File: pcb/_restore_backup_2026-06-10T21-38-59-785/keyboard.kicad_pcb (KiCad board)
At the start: 2 copper layers, 70 x 84 mm, 25 parts, among them SW1 SW_Push, SW2 SW_Push, SW3 RotaryEncoder_Switch, SW4 SW_Push, SW5 SW_Push, SW6 SW_Push, SW7 SW_Push, SW8 SW_Push, SW9 SW_Push, U1 MODULE-SEEEDUINO-XIAO-RP2040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

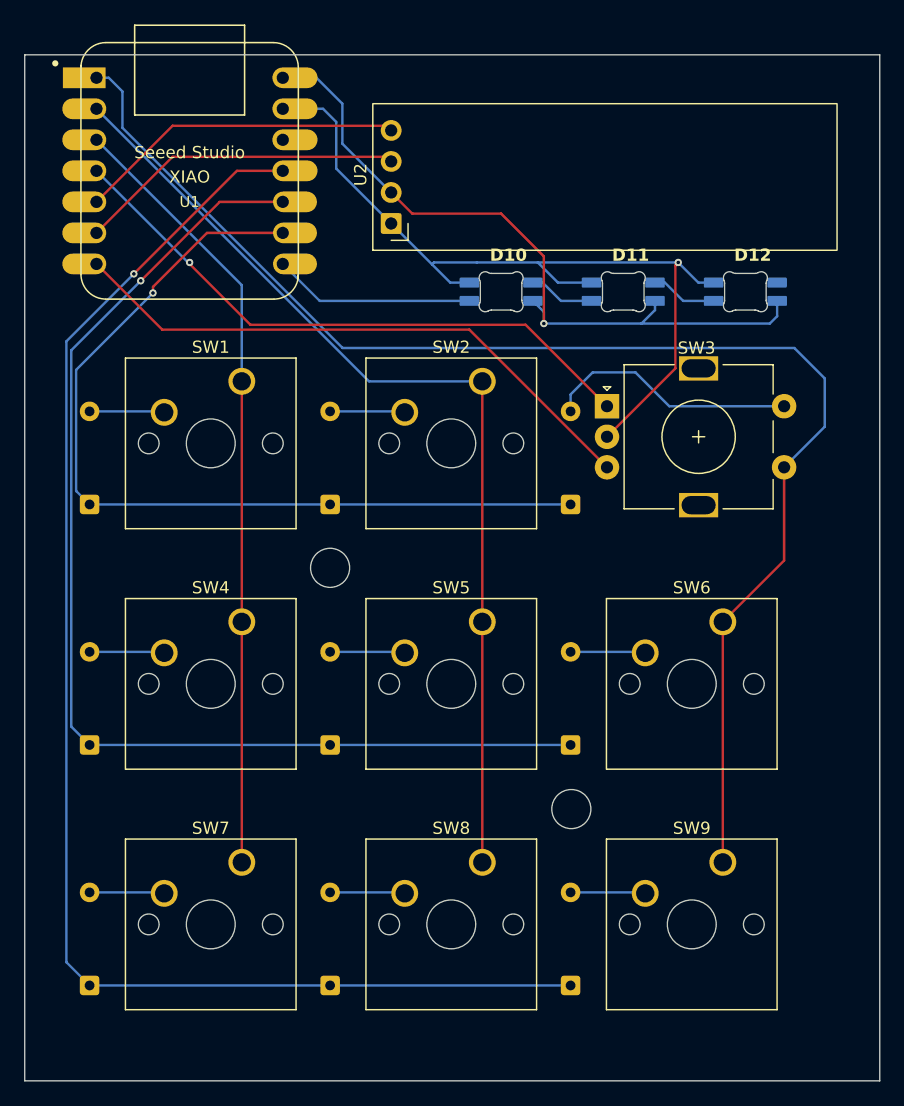
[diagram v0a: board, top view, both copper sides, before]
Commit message: connect everything on the pcb
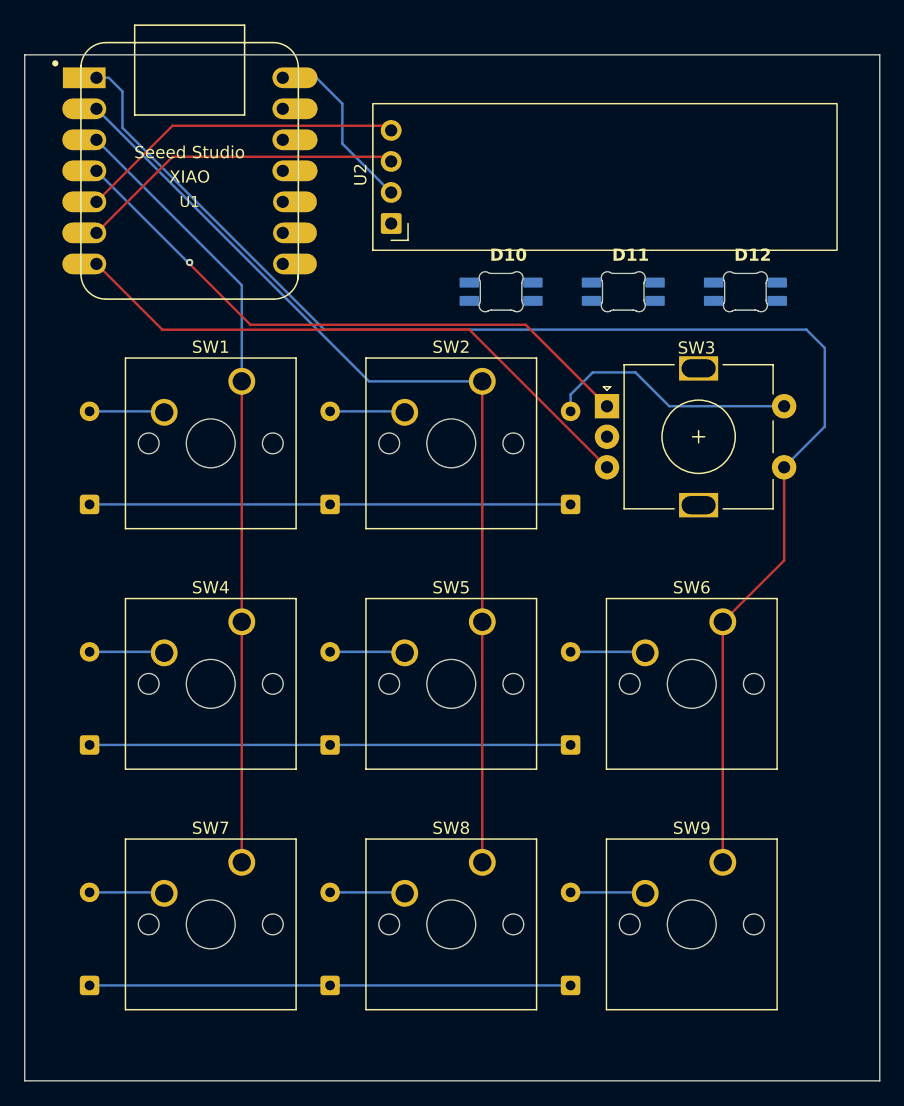
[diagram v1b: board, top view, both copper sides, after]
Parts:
- removed REF** (x2): MountingHole_3.2mm_M3, MountingHole:MountingHole_3.2mm_M3
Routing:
- net Row 2: track 116.4 -> 39.4 mm, vias 1 -> 0
- net GND: track 69.0 -> 0.00 mm, vias 1 -> 0
- net Row 1: track 94.7 -> 39.4 mm, vias 1 -> 0
- net VCC: track 60.0 -> 14.7 mm, vias 1 -> 0
- net Row 0: track 72.7 -> 39.4 mm, vias 1 -> 0
- net RGB LEDs: track 16.5 -> 0.00 mm
- net Net-(D11-DOUT): track 5.42 -> 0.00 mm
- net Net-(D10-DOUT): track 5.42 -> 0.00 mm
- net Column 2: track 114.6 -> 116.1 mm
